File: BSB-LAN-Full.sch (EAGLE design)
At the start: 120 parts, among them IC1 LAN8710A-EZC, IC2 TPS2376D, IC3 TX4138, IC4 SY8089AAAC, IC6 CH340X, Q1 BC847, Q2 BC857, Q3 BC847, Q4 WPM2015-3/TR, Q5 BC847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

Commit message: Correct ESP32 Prog Control + Update Libraries
1. Correct the control of automatic bootloader entry by adding missing resistor from GPIO2 to GPIO0.
2. Update libraries and fix layout to account for changes.
3. Change the LAN versions of the boards to use the ESP32 with external antenna. If the PCB antenna is used then it is not possible to get the PCB into the enclosure because components stick out on both ends!
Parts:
- added R51: 220R, BSB-LAN:R-EU_R0402
- ESP1: value ESP32-WROOM-32E -> ESP32-WROOM-32UE; device BSB-LAN:ESP32-WROOM-32E -> BSB-LAN:ESP32-WROOM-32UE
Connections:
- net ESP-GPIO0: now also R51.1
- net ESP-SD-DATA: now also R51.2

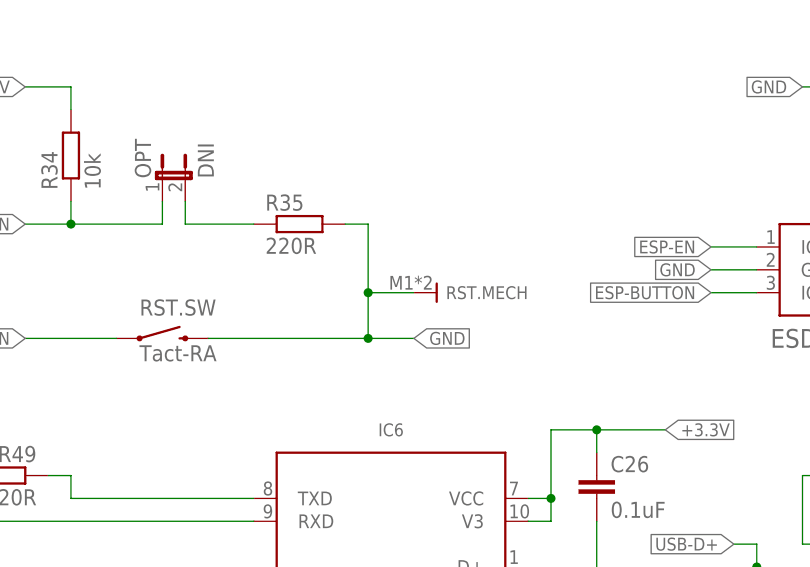
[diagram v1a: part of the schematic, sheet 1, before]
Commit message: Smaller Reset Switch on BSB-LAN-Full
Use a smaller reset switch so that it is mechanically possible to fit the board into its enclosure - we can't have components hanging over both ends of the board otherwise it won't fit into the case.
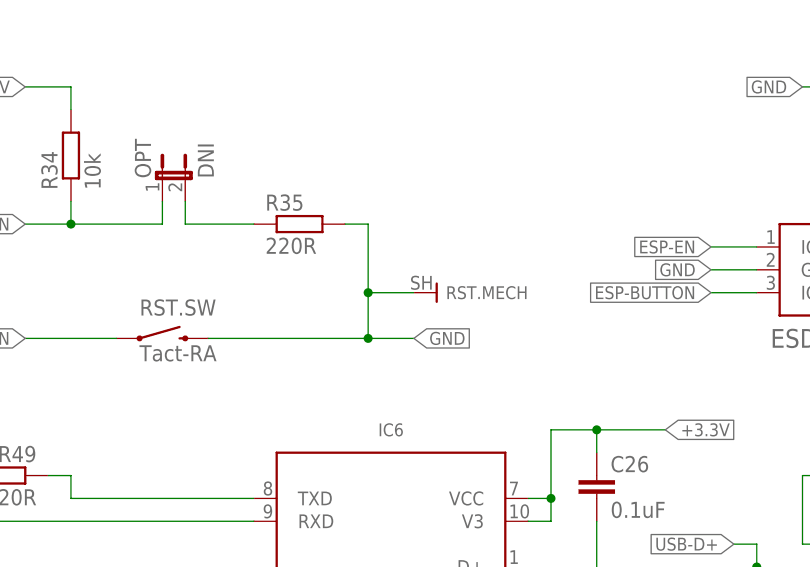
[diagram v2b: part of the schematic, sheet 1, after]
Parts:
- RST: device BSB-LAN:SWITCH-MOMENTARY-SHELL -> BSB-LAN:SWITCH-MOMENTARY-SHELL-SMD-RA; LCSC_PART C406156 -> (none)
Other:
- moved on the sheet: RST.MECH
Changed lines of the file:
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@@
 <attribute name="LCSC_PART" value="C223993"/>
 </part>
-<part name="RST" library="BSB-LAN" deviceset="SWITCH-MOMENTARY-SHELL" device="" value="Tact-RA">
-<attribute name="LCSC_PART" value="C406156"/>
-</part>
+<part name="RST" library="BSB-LAN" deviceset="SWITCH-MOMENTARY-SHELL" device="-SMD-RA" value="Tact-RA"/>
 <part name="OPT" library="BSB-LAN" deviceset="JUMPER-2" device="-2MM" value="DNI"/>
 <part name="Q5" library="BSB-LAN" deviceset="BC847*" device="" value="BC847">
